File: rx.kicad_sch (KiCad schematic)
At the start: 32 parts, among them U1 CC1200

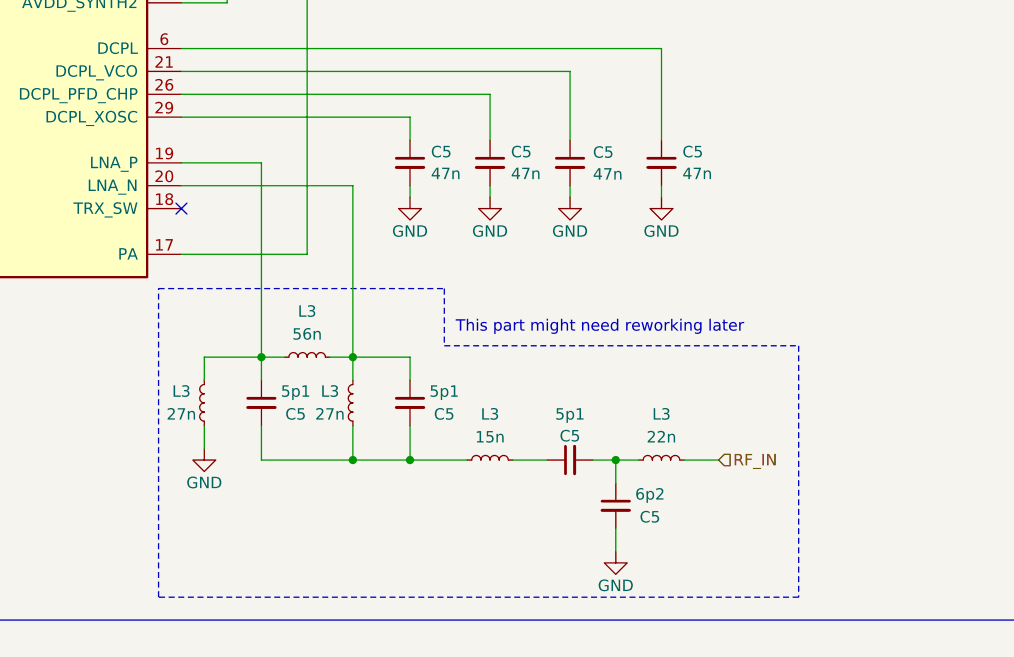
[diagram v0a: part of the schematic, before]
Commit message: significant updates
- supply for the detector block changed from 3.3V to 5V
- minor bugfixes
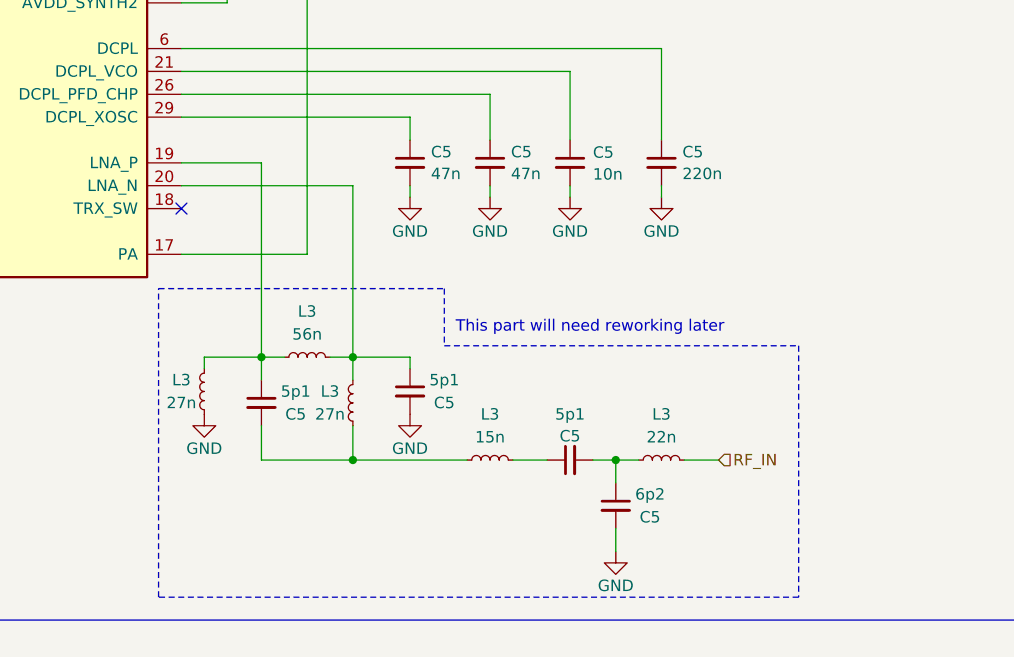
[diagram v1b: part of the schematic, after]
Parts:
- C5: value 47n -> 220n; PN C0603C473K5RACTU -> (none)
- C5: value 47n -> 10n; PN C0603C473K5RACTU -> C0603C103K5RAC7081
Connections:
- net GND: now also C5.2
- net at C5.2, L3.2, L3.2: no longer C5.2
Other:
- note added: "This part will need reworking later"
- note removed: "This part might need reworking later"
- moved on the sheet: C5, L3

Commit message: PN update
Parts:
- C5: PN (none) -> C0603C223K4RACTU
- C5: PN (none) -> GRM1885C1H9R1BA01D
- C5: PN (none) -> CC0603CRNPO9BN5R1
- C5: PN (none) -> GRM1885C1H6R2BA01D
- FB1: PN (none) -> BLM18KG601SH1D
- JP1: value ~ -> JP; PN (none) -> -
- U1: PN (none) -> CC1200RHBR
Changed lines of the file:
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@@
       (effects (font (size 1.27 1.27)) hide)
     )
-    (property "PN" "" (at 247.65 101.6 0)
+    (property "PN" "C0603C223K4RACTU" (at 247.65 101.6 0)
       (effects (font (size 1.27 1.27)) hide)
     )
@@
       (effects (font (size 1.27 1.27)))
     )
-    (property "Value" "~" (at 204.47 65.9709 0)
+    (property "Value" "JP" (at 204.47 65.9709 0)
       (effects (font (size 1.27 1.27)))
     )
@@
       (effects (font (size 1.27 1.27)) hide)
     )
+    (property "PN" "-" (at 204.47 68.58 0)
+      (effects (font (size 1.27 1.27)) hide)
+    )
     (pin "1")
     (pin "2")
@@
       (effects (font (size 1.27 1.27)) hide)
     )
-    (property "PN" "" (at 152.4 93.98 0)
+    (property "PN" "GRM1885C1H9R1BA01D" (at 152.4 93.98 0)
       (effects (font (size 1.27 1.27)) hide)
     )
@@
       (effects (font (size 1.27 1.27)) hide)
     )
+    (property "PN" "CC0603CRNPO9BN5R1" (at 203.2 128.27 0)
+      (effects (font (size 1.27 1.27)) hide)
+    )
     (pin "1")
     (pin "2")
@@
       (effects (font (size 1.27 1.27)) hide)
     )
+    (property "PN" "CC0603CRNPO9BN5R1" (at 219.71 127 0)
+      (effects (font (size 1.27 1.27)) hide)
+    )
     (pin "1")
     (pin "2")
@@
       (effects (font (size 1.27 1.27)) hide)
     )
+    (property "PN" "CC0603CRNPO9BN5R1" (at 237.49 134.62 0)
+      (effects (font (size 1.27 1.27)) hide)
+    )
     (pin "1")
     (pin "2")
@@
       (effects (font (size 1.27 1.27)) hide)
     )
+    (property "PN" "GRM1885C1H6R2BA01D" (at 242.57 139.7 0)
+      (effects (font (size 1.27 1.27)) hide)
+    )
     (pin "1")
     (pin "2")
@@
     )
     (property "Datasheet" "http://www.ti.com/lit/ds/symlink/cc1200.pdf" (at 163.83 57.15 0)
+      (effects (font (size 1.27 1.27)) hide)
+    )
+    (property "PN" "CC1200RHBR" (at 176.53 86.36 0)
       (effects (font (size 1.27 1.27)) hide)
     )
@@
       (effects (font (size 1.27 1.27)) hide)
     )
-    (property "PN" "" (at 201.93 200.66 90)
-      (effects (font (size 1.27 1.27)) hide)
-    )
+    (property "PN" "BLM18KG601SH1D" (at 201.93 200.66 90)
+      (effects (font (size 1.27 1.27)) hide)
+    )

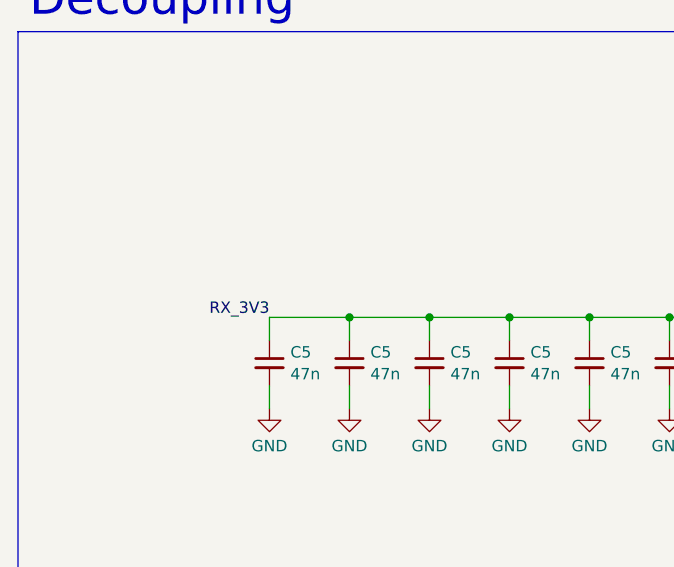
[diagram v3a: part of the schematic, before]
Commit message: `PWR_FLAG`, ERC cleanup
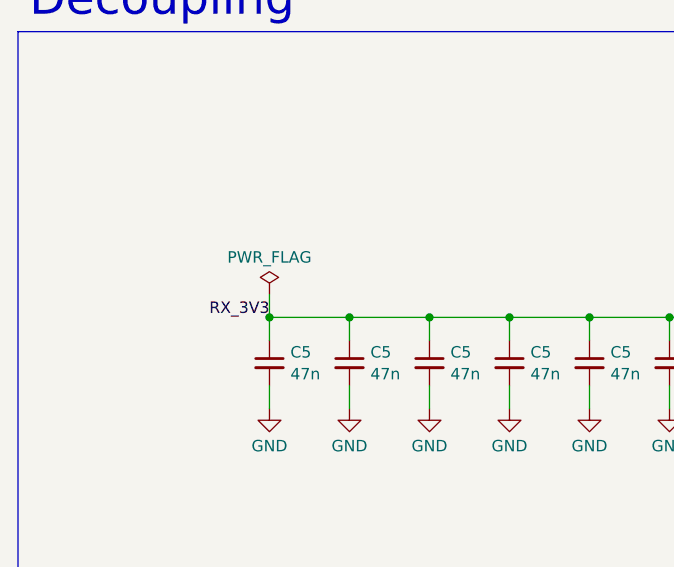
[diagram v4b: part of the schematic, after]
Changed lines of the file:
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@@
     (comment 1 "Wojciech Kaczmarski, SP5WWP")
+  )
+  (junction (at 124.46 200.66) (diameter 0) (color 0 0 0 0)
   )
   (junction (at 213.36 123.19) (diameter 0) (color 0 0 0 0)
@@
     (stroke (width 0) (type default))
   )
+  (wire (pts (xy 124.46 198.12) (xy 124.46 200.66))
+    (stroke (width 0) (type default))
+  )
   (wire (pts (xy 147.32 106.68) (xy 149.86 106.68))
     (stroke (width 0) (type default))
@@
         )
       )
+    )
+  )
+  (symbol (lib_id "power:PWR_FLAG") (at 124.46 198.12 0) (unit 1)
+    (in_bom yes) (on_board yes) (dnp no) (fields_autoplaced)
+    (property "Reference" "#FLG01" (at 124.46 196.215 0)
+      (effects (font (size 1.27 1.27)) hide)
+    )
+    (property "Value" "PWR_FLAG" (at 124.46 193.9869 0)
+      (effects (font (size 1.27 1.27)))
+    )
+    (property "Footprint" "" (at 124.46 198.12 0)
+      (effects (font (size 1.27 1.27)) hide)
+    )
+    (property "Datasheet" "~" (at 124.46 198.12 0)
+      (effects (font (size 1.27 1.27)) hide)
+    )
+    (pin "1")
+    (instances
+      (project "m17-rru-rf"
+        (path "/4c42207c-9e6b-42da-ad38-da126b892014/270fa747-1697-46c9-b996-5c9733c883e2"
+          (reference "#FLG01") (unit 1)
+        )
+        (path "/4c42207c-9e6b-42da-ad38-da126b892014/67f0dbce-cbd0-480e-94dd-fb4f6a57e3e4"
+          (reference "#FLG04") (unit 1)
+        )
+      )

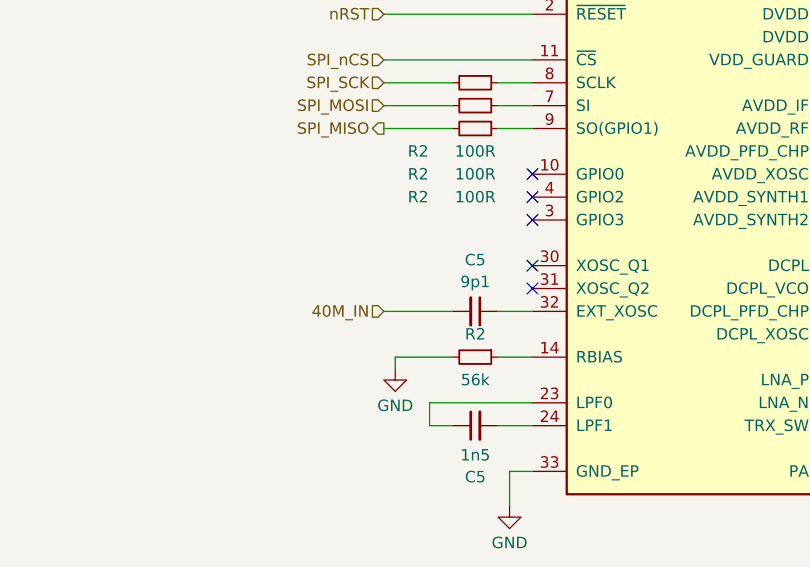
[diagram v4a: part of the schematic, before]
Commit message: TP updates, temp sensor added
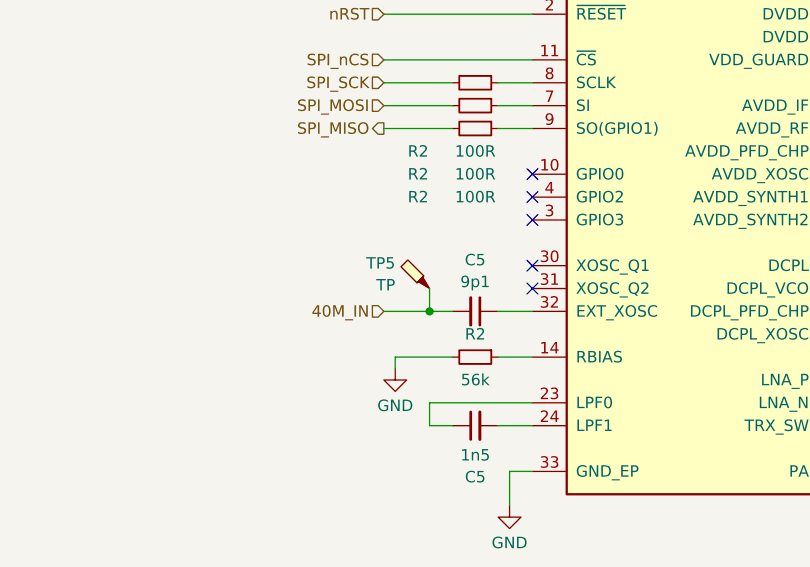
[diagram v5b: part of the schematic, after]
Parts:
- added TP5: TP, TestPoint:TestPoint_Pad_D1.5mm, symbol Connector:TestPoint_Probe
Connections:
- net 40M_IN: now also TP5.1

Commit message: date update
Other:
- title: M17 Remote Radio Unit - RF board -> Remote Radio Unit - RF board
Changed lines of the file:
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@@
   (paper "A3")
   (title_block
-    (title "M17 Remote Radio Unit - RF board")
-    (date "28-10-2023")
+    (title "Remote Radio Unit - RF board")
+    (date "30-10-2023")
     (rev "A")
     (company "M17 Project")
